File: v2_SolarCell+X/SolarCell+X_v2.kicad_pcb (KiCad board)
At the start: 6 copper layers, 48.4 x 48.4 mm, 2 parts

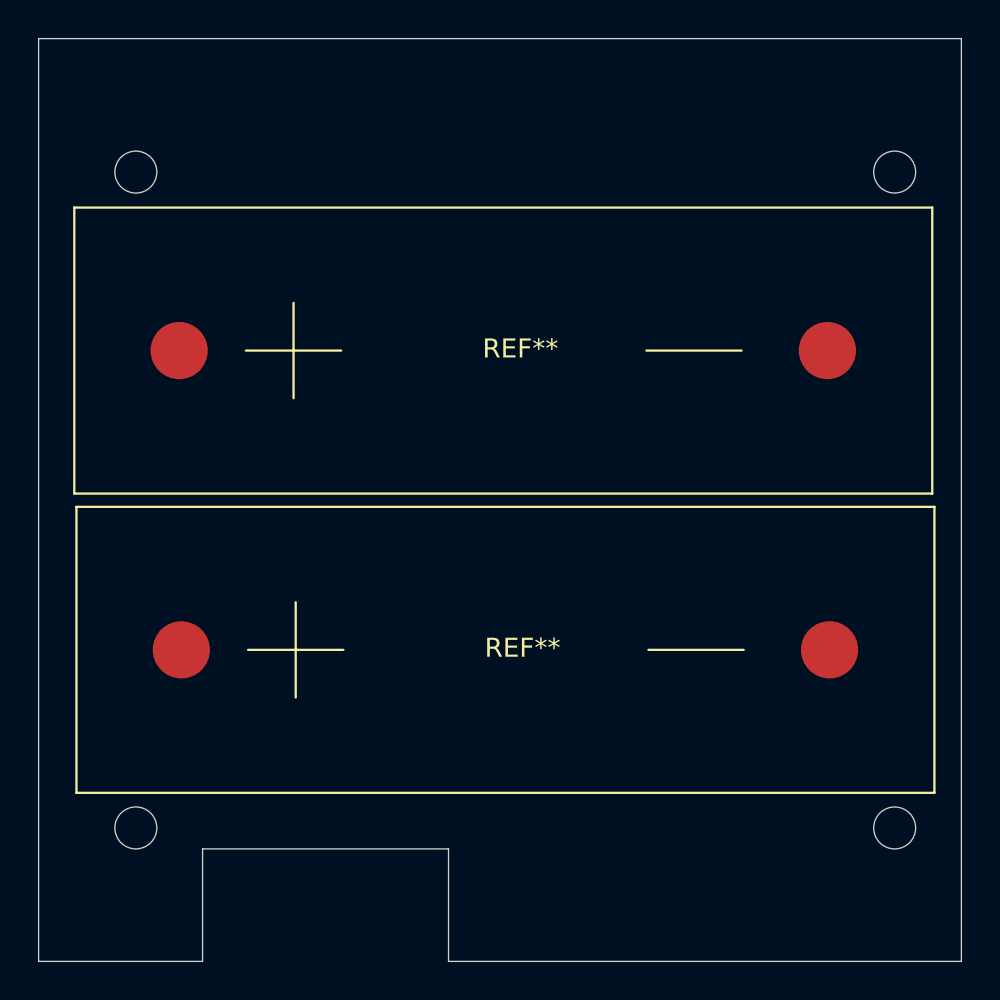
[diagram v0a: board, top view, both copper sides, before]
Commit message: Added the first layer of the magnetorquer
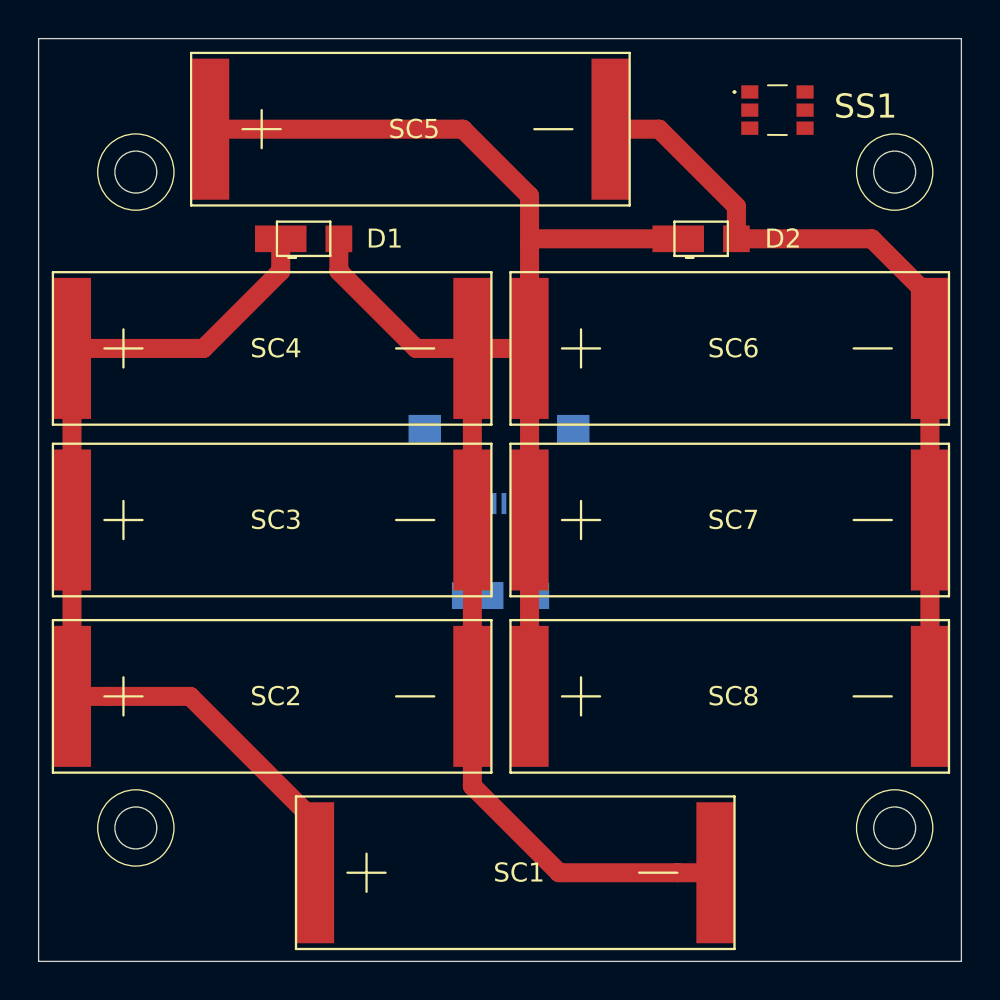
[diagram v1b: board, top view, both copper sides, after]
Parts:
- removed REF** (x2): SM141K04LV, SolarCellX:SM141K04LV
- added D1: SBDiode, SolarCellParts:SB Diode, F.Cu at (103.9, 50.5)
- added D2: SBDiode, SolarCellParts:SB Diode, F.Cu at (124.8, 50.5)
- added D3: SBDiode, SolarCellParts:SB Diode, B.Cu at (114.2, 69.2)
- added J1: symbols_XF2M-1015-1A, misc-circuits:XF2M-1015-1A, B.Cu at (114.2, 64.4)
- added SC1: SolarCell_Small, SolarCellParts:KXOB25-05X3F, F.Cu at (104.5, 83.8)
- added SC2: SolarCell_Small, SolarCellParts:KXOB25-05X3F, F.Cu at (91.8, 74.5)
- added SC3: SolarCell_Small, SolarCellParts:KXOB25-05X3F, F.Cu at (91.8, 65.2)
- added SC4: SolarCell_Small, SolarCellParts:KXOB25-05X3F, F.Cu at (91.8, 56.2)
- added SC5: SolarCell_Small, SolarCellParts:KXOB25-05X3F, F.Cu at (99.0, 44.8)
- added SC6: SolarCell_Small, SolarCellParts:KXOB25-05X3F, F.Cu at (115.8, 56.2)
- added SC7: SolarCell_Small, SolarCellParts:KXOB25-05X3F, F.Cu at (115.8, 65.2)
- added SC8: SolarCell_Small, SolarCellParts:KXOB25-05X3F, F.Cu at (115.8, 74.5)
- added SS1: symbols_TSL2561, misc-circuits:TSL2561, F.Cu at (128.8, 43.8)
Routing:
- net Net-(D1-Pad2): track 0.00 -> 103.3 mm
- net Net-(D1-Pad1): track 0.00 -> 50.7 mm
- net Net-(D2-Pad2): track 0.00 -> 42.3 mm
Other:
- outline, holes or cut-outs redrawn
